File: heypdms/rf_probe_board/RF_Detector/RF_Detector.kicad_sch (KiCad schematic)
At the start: 43 parts, among them J2 CONN_2x3_Shrouded, U1 LP3985, U2 AD8361, U3 ADS1100

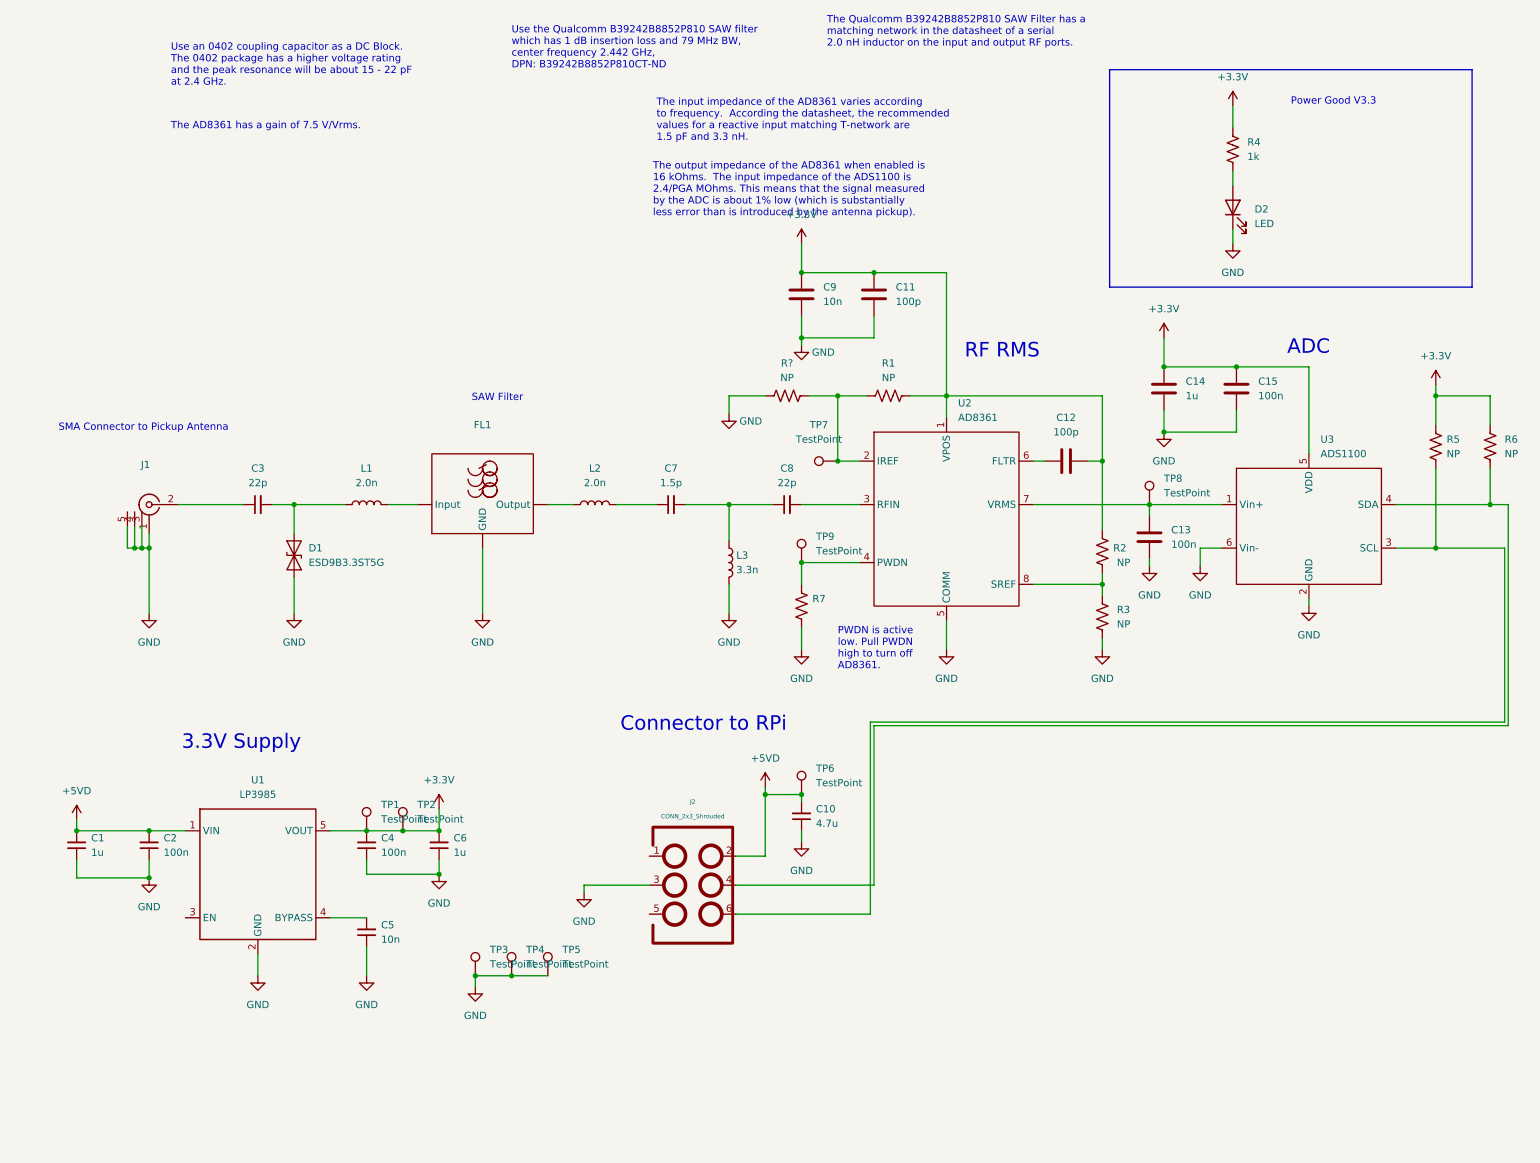
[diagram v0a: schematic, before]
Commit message: Needs the 2x3 connector to be a 2mm pitch.   The pcb is started.
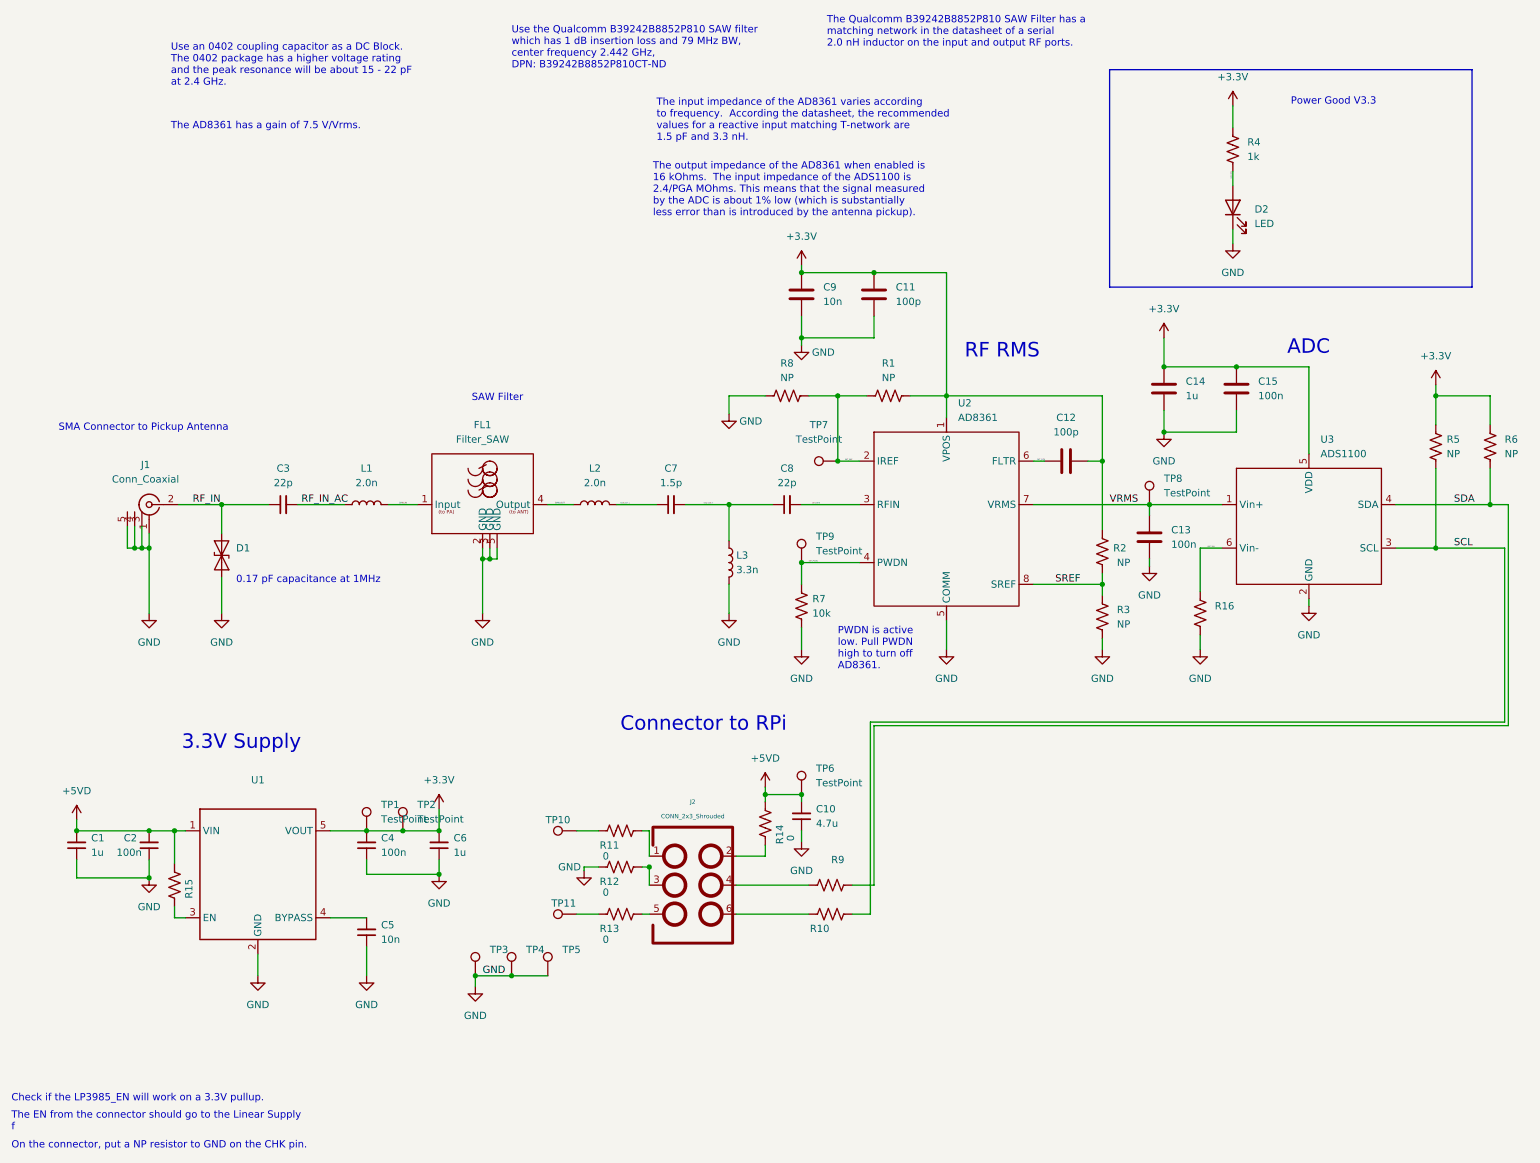
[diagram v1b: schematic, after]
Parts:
- added R10, R15, R16, R9: (no value), symbol Device:R_US
- added R11, R12, R13, R14: 0, Resistor_SMD:R_0402_1005Metric, symbol Device:R_US
- added TP10, TP11: (no value), symbol Connector:TestPoint
- C1, C11, C12, C13, C14, C15, C2, C3, C4, C5, C6, C8, C9: footprint (none) -> Capacitor_SMD:C_0402_1005Metric
- C10: footprint (none) -> Capacitor_SMD:C_1206_3216Metric
- C7: footprint (none) -> Capacitor_SMD:C_0201_0603Metric
- D1: value ESD9B3.3ST5G -> (none); footprint Diode_SMD:D_SOD-923 -> (none)
- FL1: value (none) -> Filter_SAW; footprint (none) -> rf_detector:5-SMD
- J1: value (none) -> Conn_Coaxial; footprint (none) -> rf_detector:conn_sma_endlaunch_female_062
- J2: footprint (none) -> rf_detector:CONN_2x3_100mil_shrouded_TH_75869-131
- L1, L2, L3: footprint (none) -> Inductor_SMD:L_0402_1005Metric
- R1, R2, R3, R4, R5, R6: footprint (none) -> Resistor_SMD:R_0402_1005Metric
- R7: value (none) -> 10k; footprint (none) -> Resistor_SMD:R_0402_1005Metric
- TP1, TP2, TP6, TP7, TP8: footprint (none) -> rf_detector:testpoint_1.0mm
- TP3, TP4, TP5: value TestPoint -> (none)
- U1: value LP3985 -> (none)
- U2: footprint (none) -> rf_detector:8-MSOP
- U3: footprint (none) -> Package_TO_SOT_SMD:SOT-23-6
- gave numbers to parts that had none: 1
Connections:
- net GND: now also FL1.2 (GND), FL1.3 (GND), FL1.5 (GND), R12.1, R16.1; no longer FL1. (Output), J2.3, U3.6 (Vin-)
- net SREF: now reaches R2.1, R3.2, U2.8 (SREF)
- net LED_3V3: now reaches D2.2 (A), R4.2
- net SAW_IN: now reaches L1.2
- net SAW_IN: now also FL1.1 (Input); no longer FL1. (Output)
- net SAW_OUT: now reaches L2.1
- net SAW_OUT: now also FL1.4 (Output); no longer FL1. (Output)
- net SAW_OUT_L: now reaches C7.1, L2.2
- net SAW_OUT_T: now reaches C7.2, C8.1, L3.1
- net at J2.1: now also R11.2
- net SDA: now reaches R6.2, U3.4 (SDA)
- net SDA: now also R9.2; no longer J2.4
- net at J2.5: now also R13.2
- net SCL: now reaches R5.2, U3.3 (SCL)
- net SCL: now also R10.2; no longer J2.6
- net DET_IREF: now reaches R1.1, R8.2, TP7.1, U2.2 (IREF)
- net VRMS: now reaches C13.1, TP8.1, U2.7 (VRMS), U3.1 (Vin+)
- net at U1.3 (EN): now also R15.1
- net DET_PWDN: now reaches R7.1, TP9.1, U2.4 (PWDN)
- net DET_RFIN: now reaches C8.2, U2.3 (RFIN)
- net RF_IN_AC: now reaches C3.2, L1.1
- net RF_IN_AC: no longer D1.2 (A2)
- net DET_FLTR: now reaches C12.1, U2.6 (FLTR)
- net RF_IN: now reaches C3.1, J1.2 (In)
- net RF_IN: now also D1.2 (A2)
- net +5VD: no longer names the net of C1.2, C2.2, U1.1 (VIN)
- net +5VD: now also R15.2; no longer C10.2, J2.2, TP6.1
- new net: C10.2, R14.2, TP6.1
- new net: R13.1, TP11.1
- new net: J2.2, R14.1
- new net: J2.3, R12.2
- new net: J2.4, R9.1
- new net: J2.6, R10.1
- new net: R11.1, TP10.1
- new net ADC_VIN-: R16.2, U3.6 (Vin-)
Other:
- note added: "0.17 pF capacitance at 1MHz"
- note added: "Check if the LP3985_EN will work on a 3.3V pullup."
- note added: "On the connector, put a NP resistor to GND on the CHK pin."
- note added: "The EN from the connector should go to the Linear Supply f"
- moved on the sheet: C3, D1

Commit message: RF_Detector board with zero airwires and most of the silkscreen
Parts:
- removed TP1: TestPoint, rf_detector:testpoint_1.0mm, symbol Connector:TestPoint
- removed TP3, TP4, TP5: (no value), symbol Connector:TestPoint
- added C16: 100n, Capacitor_SMD:C_0402_1005Metric, symbol Device:C_Small
- added D3: LED, Diode_SMD:D_0603_1608Metric, symbol Device:LED
- added R17: 0, Resistor_SMD:R_0402_1005Metric, symbol Device:R_US
- added TVS1, TVS2: TPD2E1B06, Package_TO_SOT_SMD:SOT-23-6, symbol RF_Detector:TPD2E1B06
- added V5D1, V5D3: V5D, symbol RF_Detector:V5D
- added V5D2: (no value), symbol RF_Detector:V5D
- D1: value (none) -> ESDL2011PFCT5G; footprint (none) -> Capacitor_SMD:C_0201_0603Metric
- D2: Color (none) -> GRN
- J2: footprint rf_detector:CONN_2x3_100mil_shrouded_TH_75869-131 -> rf_detector:CONN_2x3_2mm_shrouded_TH
- R10, R16, R9: value (none) -> 0; footprint (none) -> Resistor_SMD:R_0402_1005Metric
- R12: footprint Resistor_SMD:R_0402_1005Metric -> Resistor_SMD:R_0603_1608Metric
- R13: value 0 -> NP
- R14: value 0 -> 3.3k; Colo (none) -> GRN
- R15: value (none) -> NP; footprint (none) -> Resistor_SMD:R_0402_1005Metric
- TP10, TP11: value (none) -> TestPoint; footprint (none) -> rf_detector:testpoint_1.0mm
- U1: value (none) -> LP3985; footprint (none) -> Package_TO_SOT_SMD:SOT-23-5
- U3: value ADS1100 -> ADS1100X
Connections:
- net GND: now also C16.1, D3.1 (K), TVS1.4 (IOB2), TVS1.5 (IOE2), TVS2.4 (IOB2), TVS2.5 (IOE2)
- net VRMS: now also R17.1; no longer U2.7 (VRMS)
- net V5D: now reaches C10.2, TP6.1
- net V5D: now also C1.2, C2.2, J2.2, R14.1, R15.2, U1.1 (VIN), V5D1. (V5D), V5D2. (V5D), V5D3. (V5D); no longer R14.2
- net CHK: now reaches R13.1, TP11.1
- net LP3985_BYP: now reaches C5.2, U1.4 (BYPASS)
- net CONN_EN: now reaches J2.1, R11.2
- net CONN_EN: now also TVS1.1 (IOA1)
- net GND_CONN: now reaches J2.3, R12.2
- net SDA_CONN: now reaches J2.4, R9.1
- net SDA_CONN: now also TVS2.1 (IOA1)
- net CHK_CONN: now reaches J2.5, R13.2
- net CHK_CONN: now also TVS1.2 (IOB1)
- net SCL_CONN: now reaches J2.6, R10.1
- net SCL_CONN: now also TVS2.2 (IOB1)
- net LP3985_EN: now reaches R15.1, U1.3 (EN)
- net LP3985_EN: now also R11.1, TP10.1, C16.2
- new net LED_V5D: D3.2 (A), R14.2
- new net VRMS_UNFILTERED: R17.2, U2.7 (VRMS)
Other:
- note added: "Check that there is no collision on the I2C bus. Choose a high number I2C Address."
- note added: "REV_1.0"
- note added: "Raising LP3985_EN above 1.4V begins startup sequence."
- note removed: "Check if the LP3985_EN will work on a 3.3V pullup."
- note removed: "On the connector, put a NP resistor to GND on the CHK pin."
- note removed: "The EN from the connector should go to the Linear Supply f"
- moved on the sheet: C1, C10, C11, C12, C2, C4, C5, C6, C7, C8, C9, D2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
